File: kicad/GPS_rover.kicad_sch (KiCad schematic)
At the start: 15 parts, among them J201 SMA, J202 NormallyClosed, U201 ZED_F9R, Y401 ANN-MB-00

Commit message: Updated to KiCad 7.0
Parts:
- J201: Number in cart 1 -> (none); Number on hand 0 -> 1

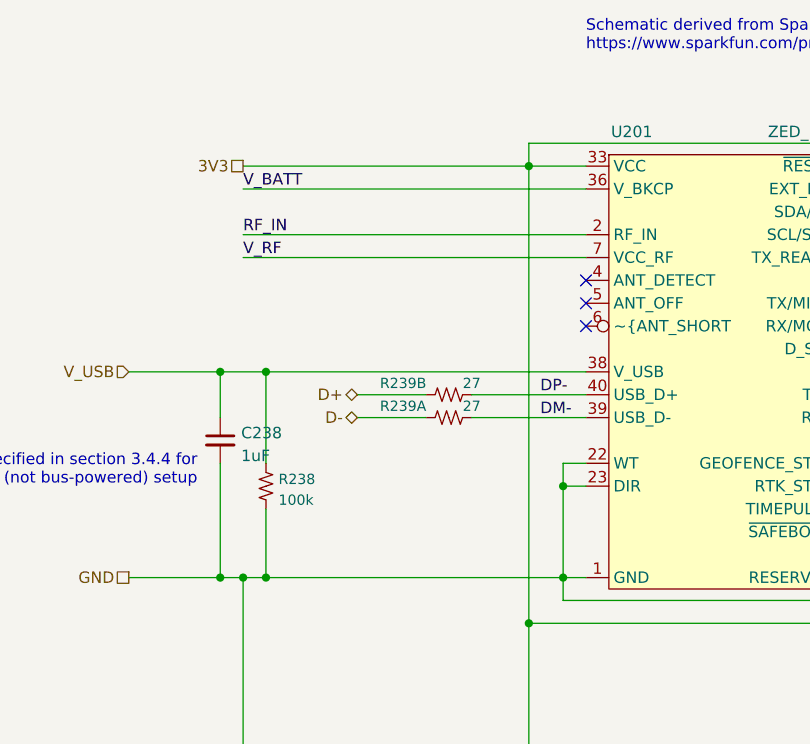
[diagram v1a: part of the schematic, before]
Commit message: Improved grounding and bypass caps on GPS
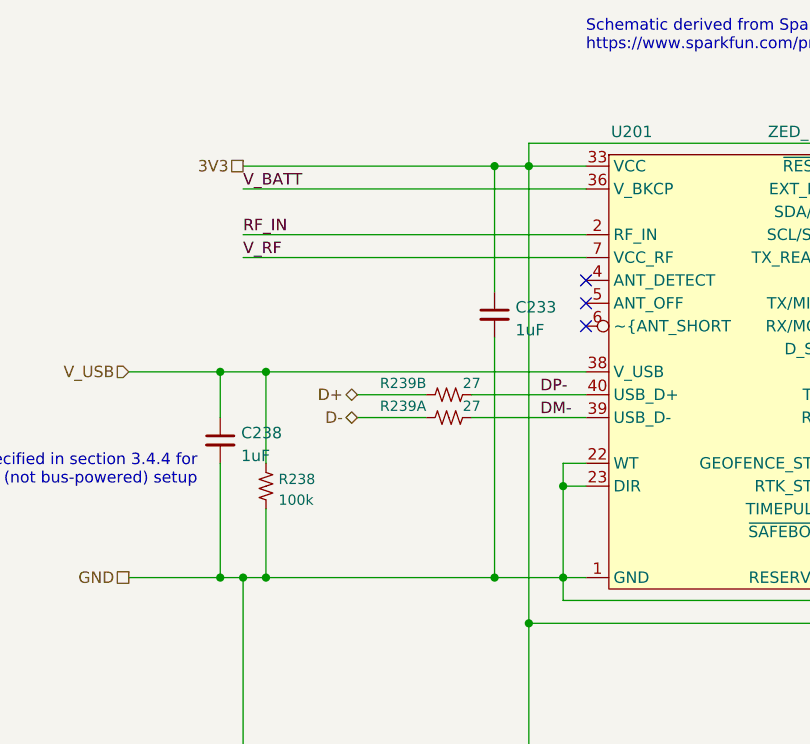
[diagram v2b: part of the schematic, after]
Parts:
- added C233: 1uF, Capacitor_SMD:C_0402_1005Metric, symbol Device:C_Small
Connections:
- net 3V3: now also C233.1
- net GND: now also C233.2
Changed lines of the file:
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@@
   (junction (at 107.95 162.56) (diameter 0) (color 0 0 0 0)
   )
+  (junction (at 104.14 50.8) (diameter 0) (color 0 0 0 0)
+  )
   (junction (at 120.65 162.56) (diameter 0) (color 0 0 0 0)
   )
@@
   )
   (junction (at 156.21 149.86) (diameter 0) (color 0 0 0 0)
+  )
+  (junction (at 104.14 96.52) (diameter 0) (color 0 0 0 0)
   )
   (junction (at 78.74 73.66) (diameter 0) (color 0 0 0 0)
@@
     (stroke (width 0) (type default))
   )
+  (wire (pts (xy 104.14 96.52) (xy 111.76 96.52))
+    (stroke (width 0) (type default))
+  )
   (wire (pts (xy 63.5 96.52) (xy 73.66 96.52))
     (stroke (width 0) (type default))
@@
     (stroke (width 0) (type default))
   )
-  (wire (pts (xy 78.74 96.52) (xy 111.76 96.52))
+  (wire (pts (xy 104.14 69.85) (xy 104.14 96.52))
+    (stroke (width 0) (type default))
+  )
+  (wire (pts (xy 78.74 96.52) (xy 104.14 96.52))
     (stroke (width 0) (type default))
   )
@@
     (stroke (width 0) (type default))
   )
+  (wire (pts (xy 104.14 50.8) (xy 107.95 50.8))
+    (stroke (width 0) (type default))
+  )
   (wire (pts (xy 165.1 88.9) (xy 144.78 88.9))
     (stroke (width 0) (type default))
@@
     (stroke (width 0) (type default))
   )
+  (wire (pts (xy 104.14 50.8) (xy 104.14 64.77))
+    (stroke (width 0) (type default))
+  )
   (wire (pts (xy 156.21 149.86) (xy 175.26 149.86))
     (stroke (width 0) (type default))
@@
     (stroke (width 0) (type default))
   )
-  (wire (pts (xy 76.2 50.8) (xy 107.95 50.8))
+  (wire (pts (xy 76.2 50.8) (xy 104.14 50.8))
     (stroke (width 0) (type default))
   )
@@
         )
       )
+    )
+  )
+  (symbol (lib_id "Device:C_Small") (at 104.14 67.31 0) (unit 1)
+    (in_bom yes) (on_board yes) (dnp no) (fields_autoplaced)
+    (property "Reference" "C233" (at 106.4641 66.4816 0)
+      (effects (font (size 1.27 1.27)) (justify left))
+    )
+    (property "Value" "1uF" (at 106.4641 69.0185 0)
+      (effects (font (size 1.27 1.27)) (justify left))
+    )
+    (property "Footprint" "Capacitor_SMD:C_0402_1005Metric" (at 104.14 67.31 0)
+      (effects (font (size 1.27 1.27)) hide)
+    )
+    (property "Datasheet" "~" (at 104.14 67.31 0)
+      (effects (font (size 1.27 1.27)) hide)
+    )
+    (property "Purpose" "V_USBDETECT capacitor" (at 104.14 67.31 0)
+      (effects (font (size 1.27 1.27)) hide)
+    )
+    (property "Digikey" "399-C0402C105K9PAC7800CT-ND" (at 104.14 67.31 0)
+      (effects (font (size 1.27 1.27)) hide)
+    )
+    (property "Mouser" "187-CL05A105KP5NNWC" (at 104.14 67.31 0)
+      (effects (font (size 1.27 1.27)) hide)
+    )
+    (property "Number on hand" "14+10" (at 104.14 67.31 0)
+      (effects (font (size 1.27 1.27)) hide)
+    )
+    (pin "1")
+    (pin "2")
+    (instances
+      (project "rollercoasterometer_hat_sf"
+        (path "/ba8024d5-8c9d-4001-9766-31acf13004f5/87ba5914-c56a-4fb4-a4a7-475b3f4e49b8"
+          (reference "C233") (unit 1)
+        )
+      )
